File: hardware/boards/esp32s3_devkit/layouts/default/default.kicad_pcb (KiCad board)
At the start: 2 copper layers, 21 parts

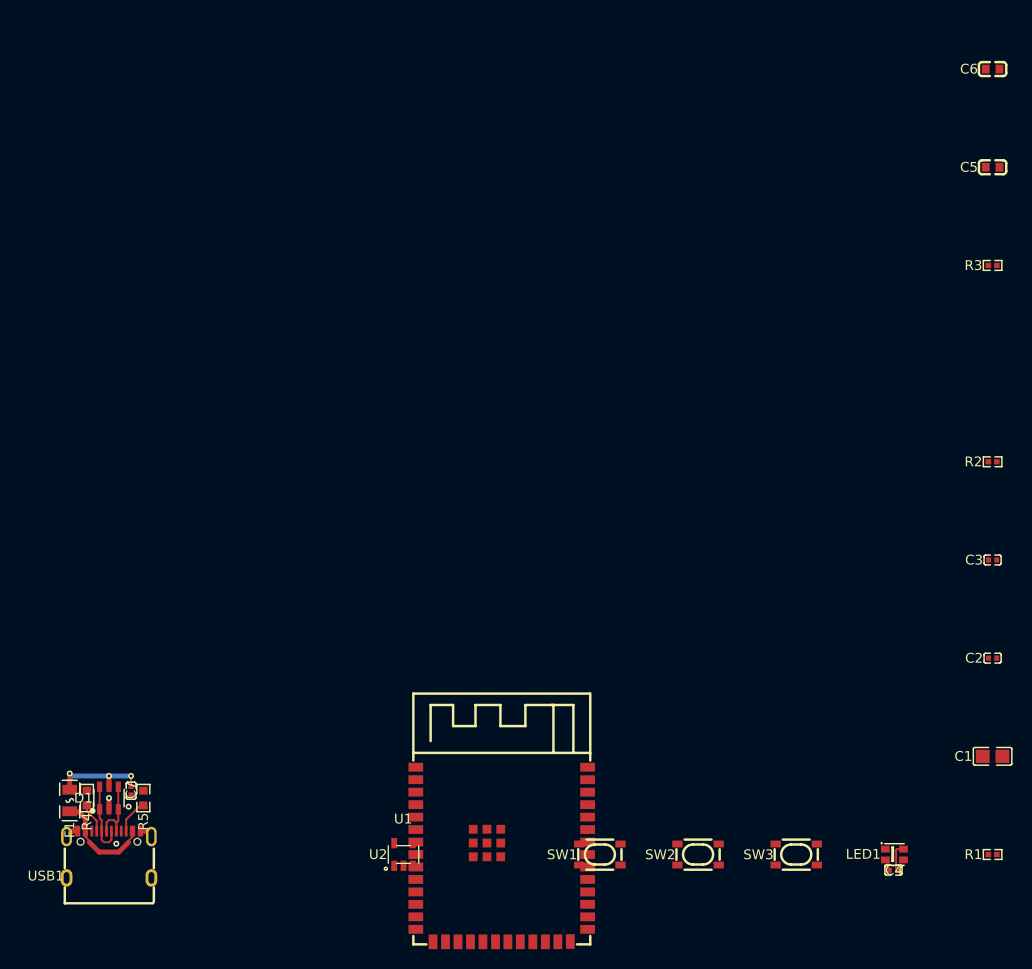
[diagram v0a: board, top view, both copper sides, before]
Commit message: feat(monorepo): vendor atopile canonical build foundation
Wire the forked atopile compiler into local development and CI so board builds emit canonical design snapshots and backend sidecars from compiler-owned contracts.

This also validates the new foundation against esp32s3_devkit and keeps the resulting KiCad layout update alongside the successful build outputs.

Made-with: Cursor
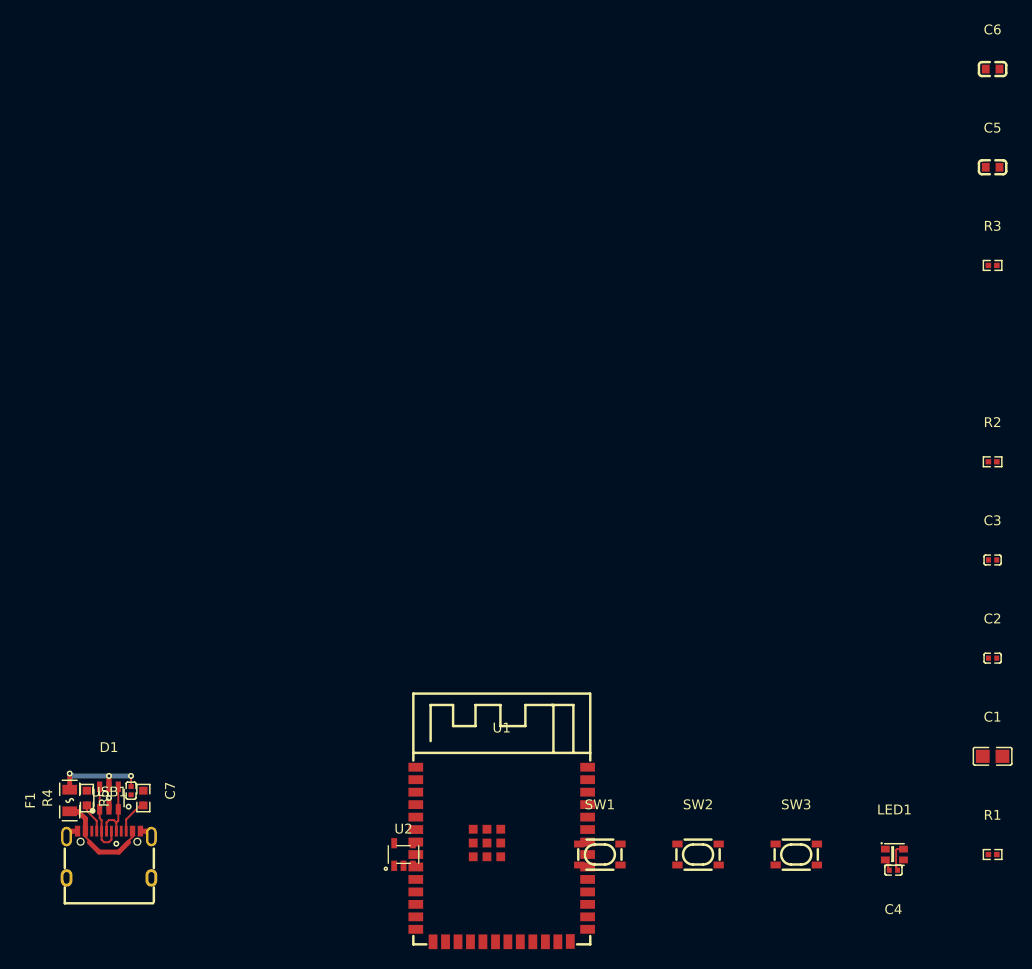
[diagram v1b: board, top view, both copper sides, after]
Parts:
- C1: value 10µF ±10% -> 10µF
- C2, C4, C7: value 100nF ±10% -> 100nF
- C3, C5, C6: value 1µF ±10% -> 1µF
- R1, R2, R3, R4, R5: value 10kΩ ±1% -> 10kΩ
